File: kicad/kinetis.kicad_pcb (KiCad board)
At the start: 2 copper layers, 88.9 x 88.9 mm, 75 parts, among them J1 USB_Micro_B, J2 JLink_SWD_20pin, J3 CONN_01X16, J4 CONN_01X16, J5 FTDI_Connector, J6 CONN_01X16, J7 CONN_01X16, M1 #4-40 Mounting Hole, M2 #4-40 Mounting Hole, M3 #4-40 Mounting Hole, M4 #4-40 Mounting Hole, SW1 DPDT, SW2 SPST, SW3 SPST, SW4 SPST, SW5 SPST, SW6 SPST, U1 LM1117-ADJ, U2 MKL16Z64VLH4, Y1 12.000 MHz

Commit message: More routing tweaks
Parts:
- moved R28 0.70 mm to (179.5, 134.6)
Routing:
- net GND: track 105.0 -> 137.3 mm, vias 33 -> 42
- net /HEADER_B[12]: track 68.4 -> 69.0 mm

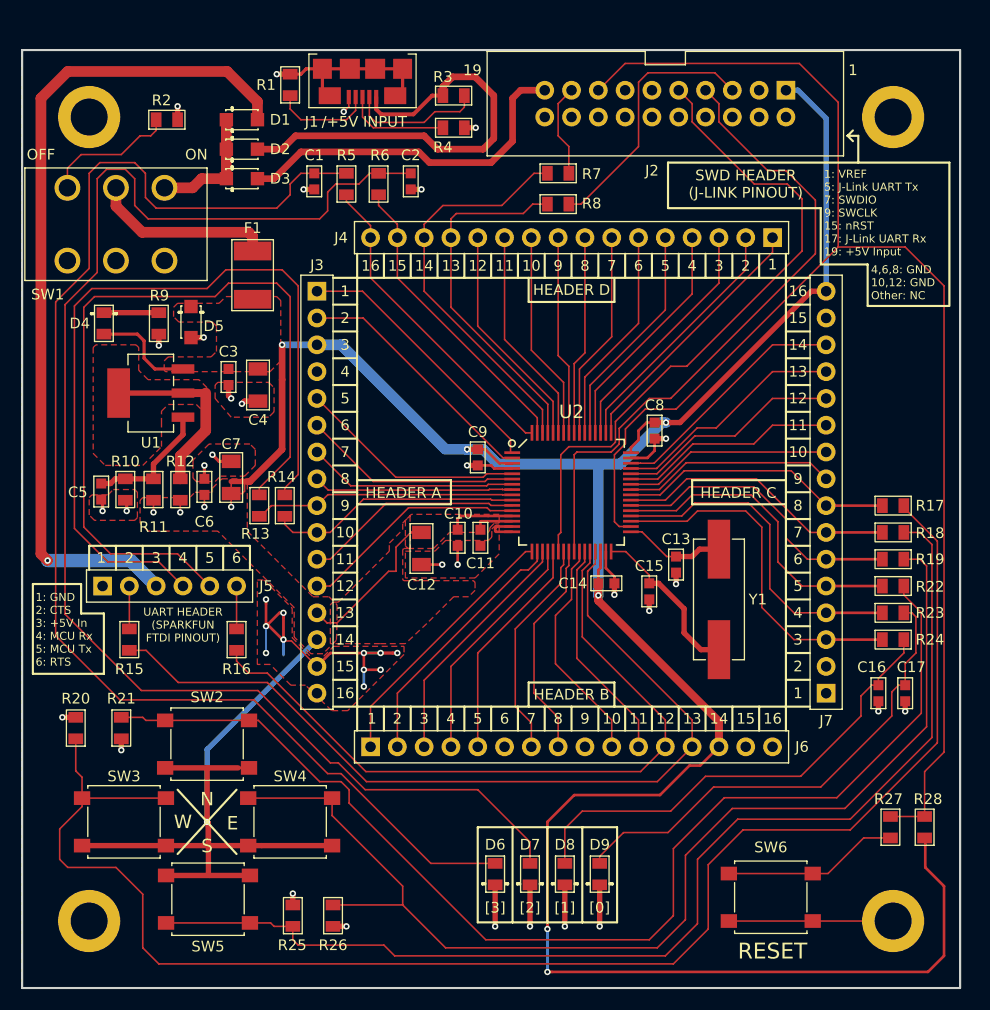
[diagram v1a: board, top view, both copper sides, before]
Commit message: Improved the +3.3V analog section
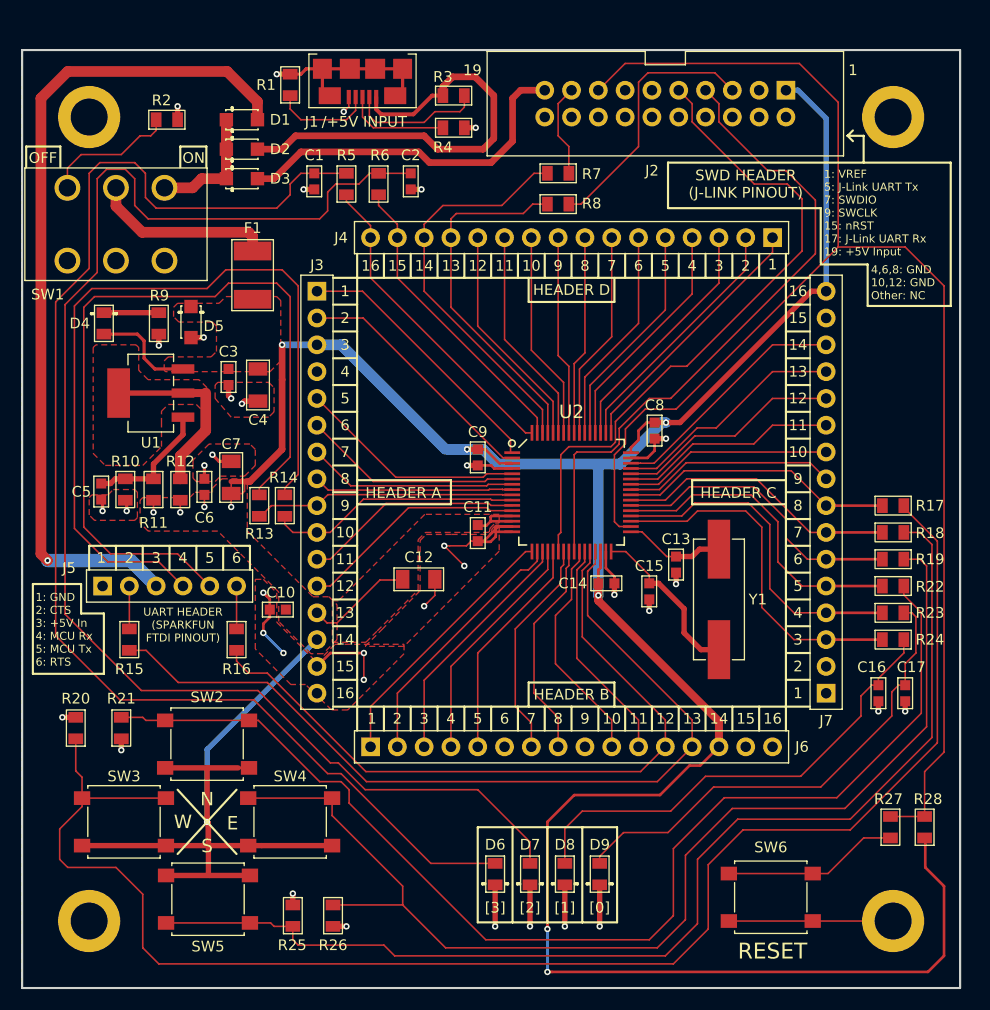
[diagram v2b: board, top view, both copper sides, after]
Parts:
- moved C10 18.4 mm to (118.2, 114.0), turned to 180 degrees
- moved C12 2.93 mm to (131.6, 111.1), turned to 0 degrees
- moved C11 0.51 mm to (137.2, 106.7)
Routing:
- net GND: track 137.3 -> 124.7 mm, vias 42 -> 37
- net +3.3V: track 337.9 -> 329.2 mm
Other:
- net class Default: clearance 0.2032 -> 0.1778
- rule trace_clearance: 0.2032 -> 0.1778

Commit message: Yet more tweaks
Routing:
- net GND: track 124.7 -> 132.4 mm, vias 37 -> 41
- net +3.3V: track 329.2 -> 324.0 mm, vias 11 -> 7

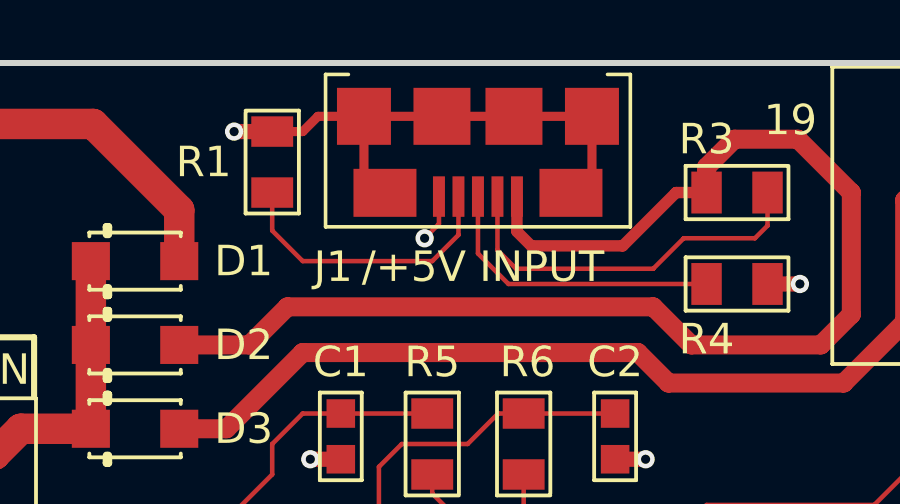
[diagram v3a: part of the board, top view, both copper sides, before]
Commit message: Updated USB 3-D model
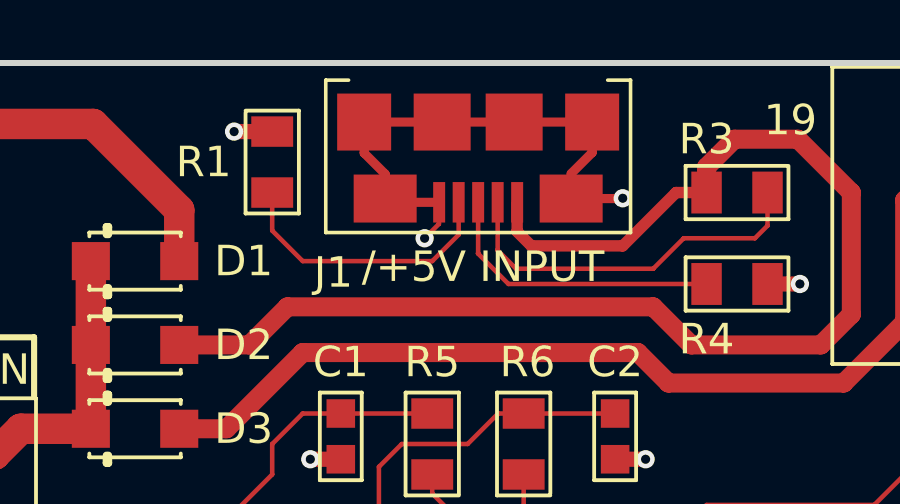
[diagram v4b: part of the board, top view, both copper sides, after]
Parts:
- moved J1 0.19 mm to (126.2, 62.9)
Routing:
- net GND: track 132.4 -> 132.8 mm, vias 41 -> 42

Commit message: Re-applied annotation
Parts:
- renumbered C5 to C1, C9 to C10, C14 to C12, C8 to C13, C15 to C14, C13 to C15, C6 to C2, C7 to C4, C4 to C5, C1 to C6, C10 to C7, C2 to C8, C12 to C9, D4 to D1, D5 to D2, D1 to D3, D2 to D4, D3 to D5, J5 to J1, J3 to J2, J1 to J3, J6 to J4, J2 to J5, J4 to J6, M3 to M2, M2 to M3, R20 to R1, R16 to R10, R13 to R11, R14 to R12, R5 to R13, R6 to R14, R25 to R15, R26 to R16, R3 to R17, R4 to R18, R7 to R19, R8 to R20, R17 to R21, R18 to R22, R19 to R23, R22 to R24, R23 to R25, R24 to R26, R10 to R3, R9 to R4, R11 to R5, R15 to R6, R21 to R7, R12 to R8, R1 to R9, SW3 to SW2, SW2 to SW3, SW5 to SW4, SW4 to SW5

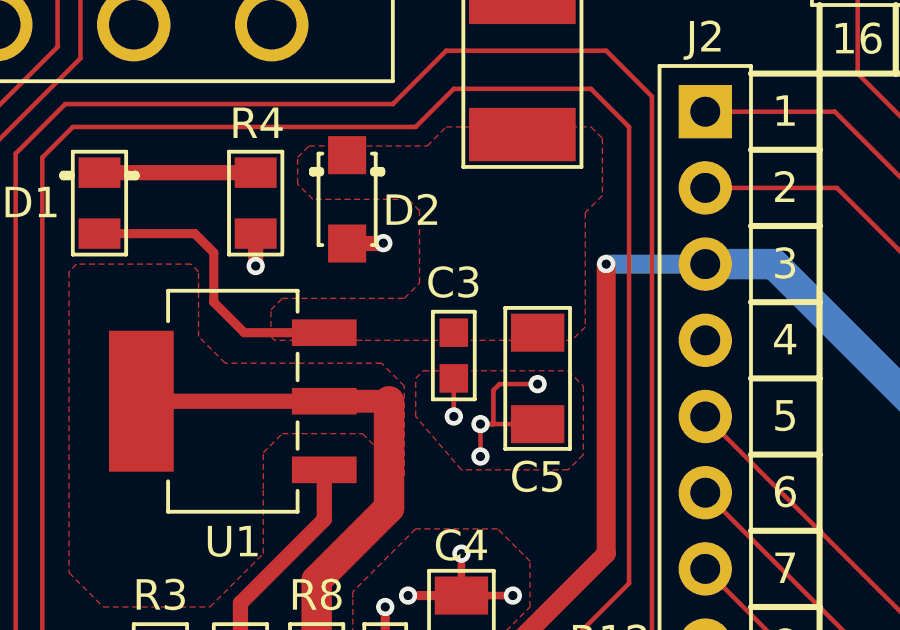
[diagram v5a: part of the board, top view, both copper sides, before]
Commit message: Updated SOD-123 footprint. Cleaned up fab drawing.
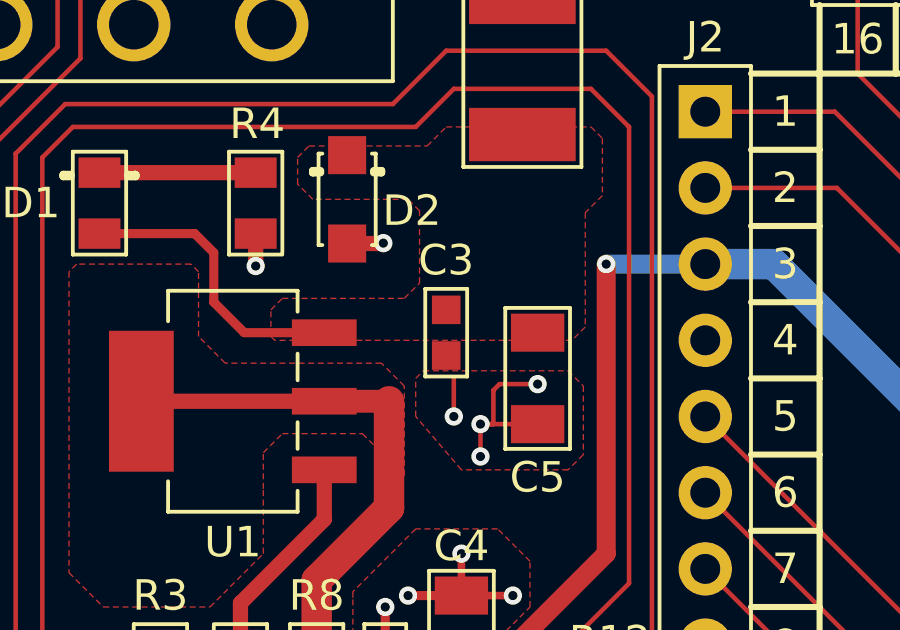
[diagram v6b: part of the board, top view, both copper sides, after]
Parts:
- moved C3 0.80 mm to (113.3, 91.2)

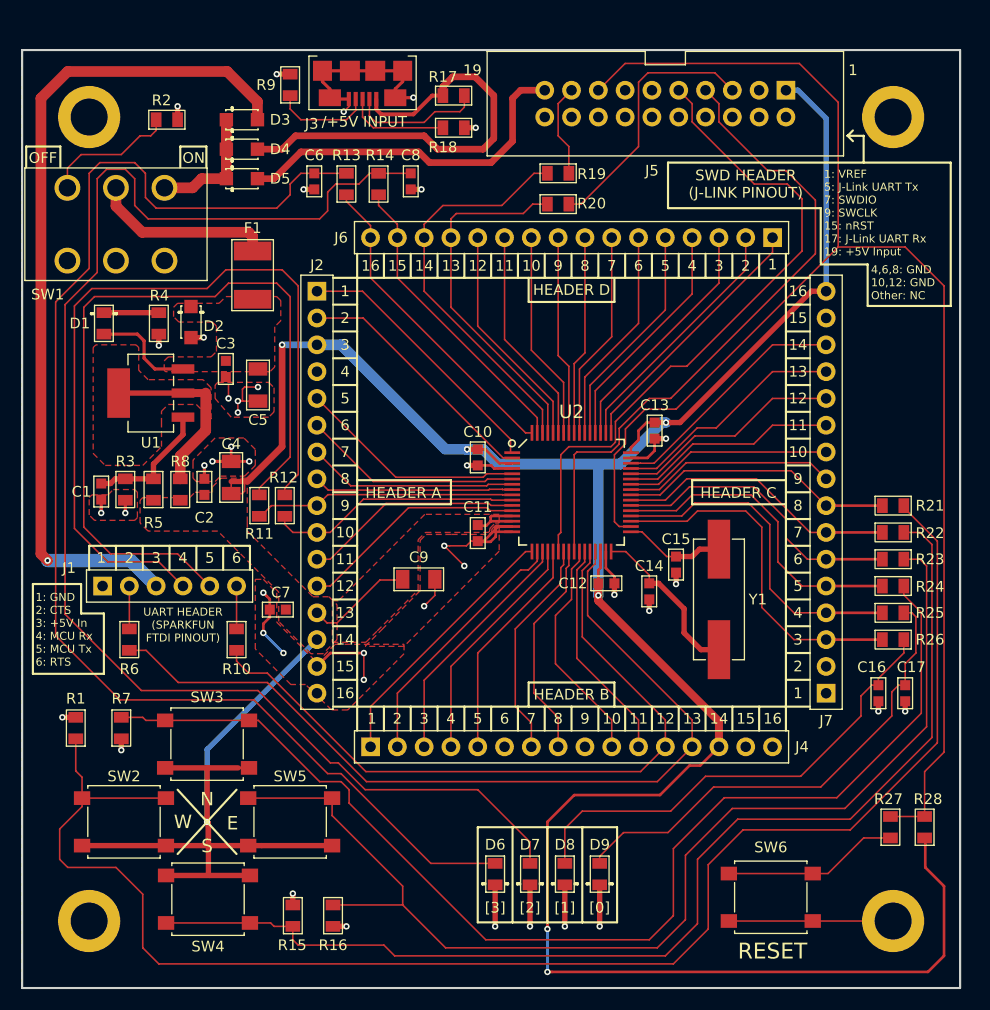
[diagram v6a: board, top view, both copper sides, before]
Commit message: Changed USB connector. Fixed soldermask clearance settings.
This commit changes the USB connector from an SMT-only connector
to one with some through-hole mounting tabs. This should help to
provide mechanical ruggedness for the board.

This commit also fixed the soldermask clearance settings so that the
USB connector and Kinets both have soldermask in-between the pins.
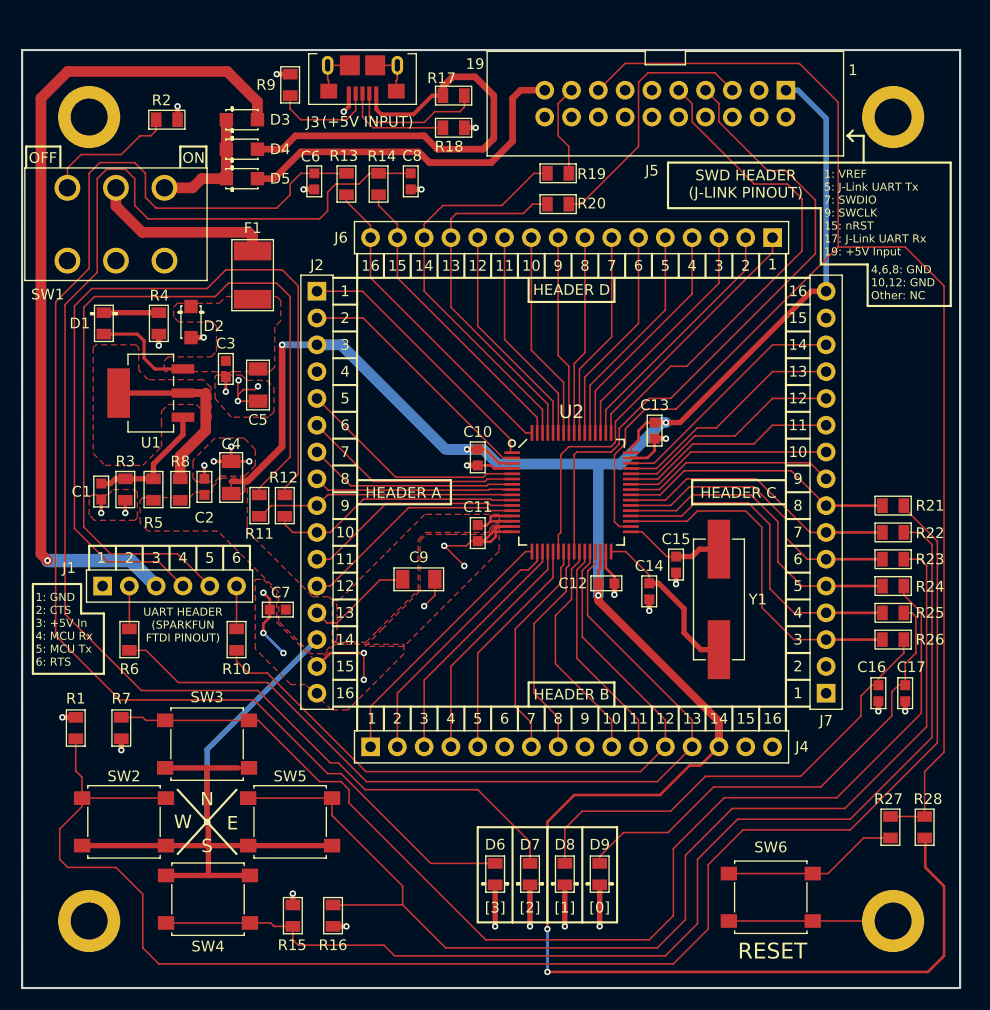
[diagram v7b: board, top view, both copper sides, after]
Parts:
- J3: footprint custom_footprints:10118192-0001LF -> custom_footprints:10118193-0001LF
- moved J3 0.52 mm to (126.2, 62.4)
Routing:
- net GND: track 132.8 -> 125.5 mm, vias 42 -> 41
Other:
- rule pad_to_mask_clearance: 0.2 -> 0.1016
- board text added: "(+5V INPUT)"
- board text removed: "/+5V INPUT"

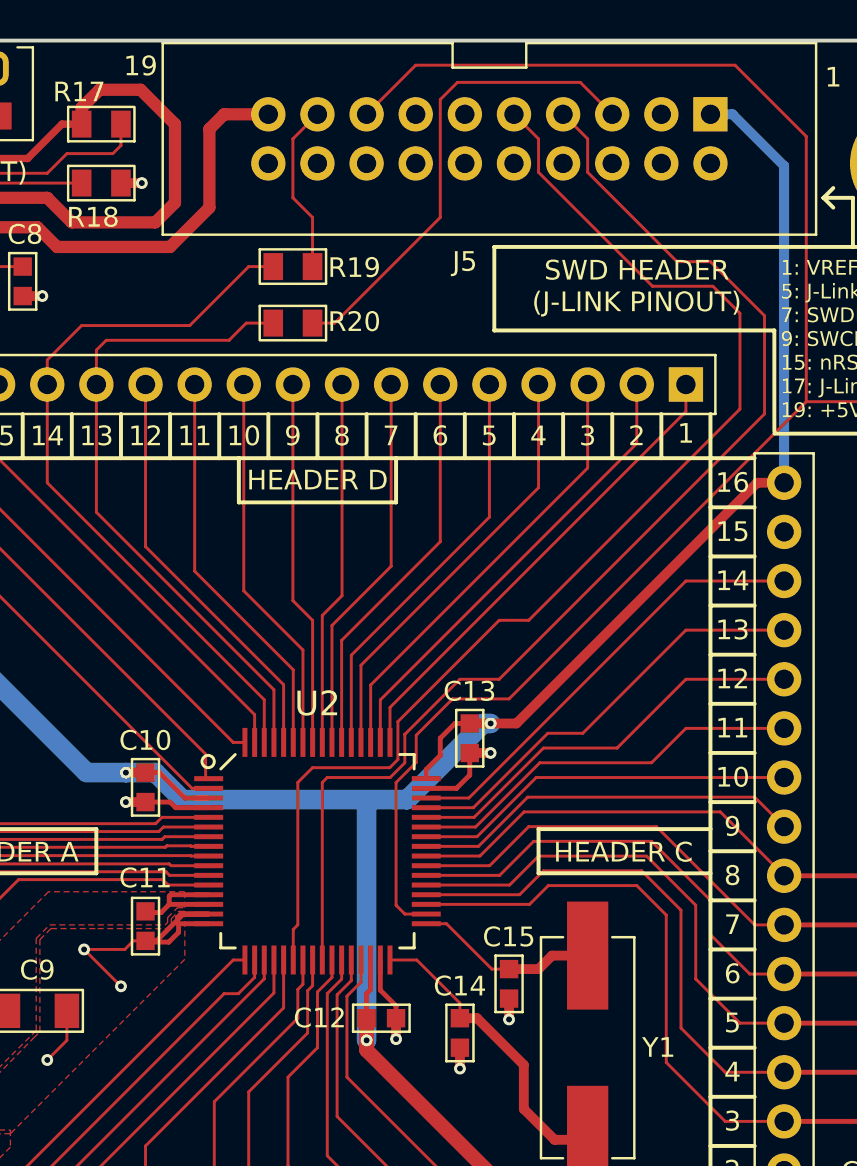
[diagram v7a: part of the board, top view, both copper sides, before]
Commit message: Bugfix to USB 3D model. Added ground stitches.
This commit fixes the selection of the USB connector's 3D model.
It also adds some small ground patches over the 3.3V disruptions
under the Kinetis.
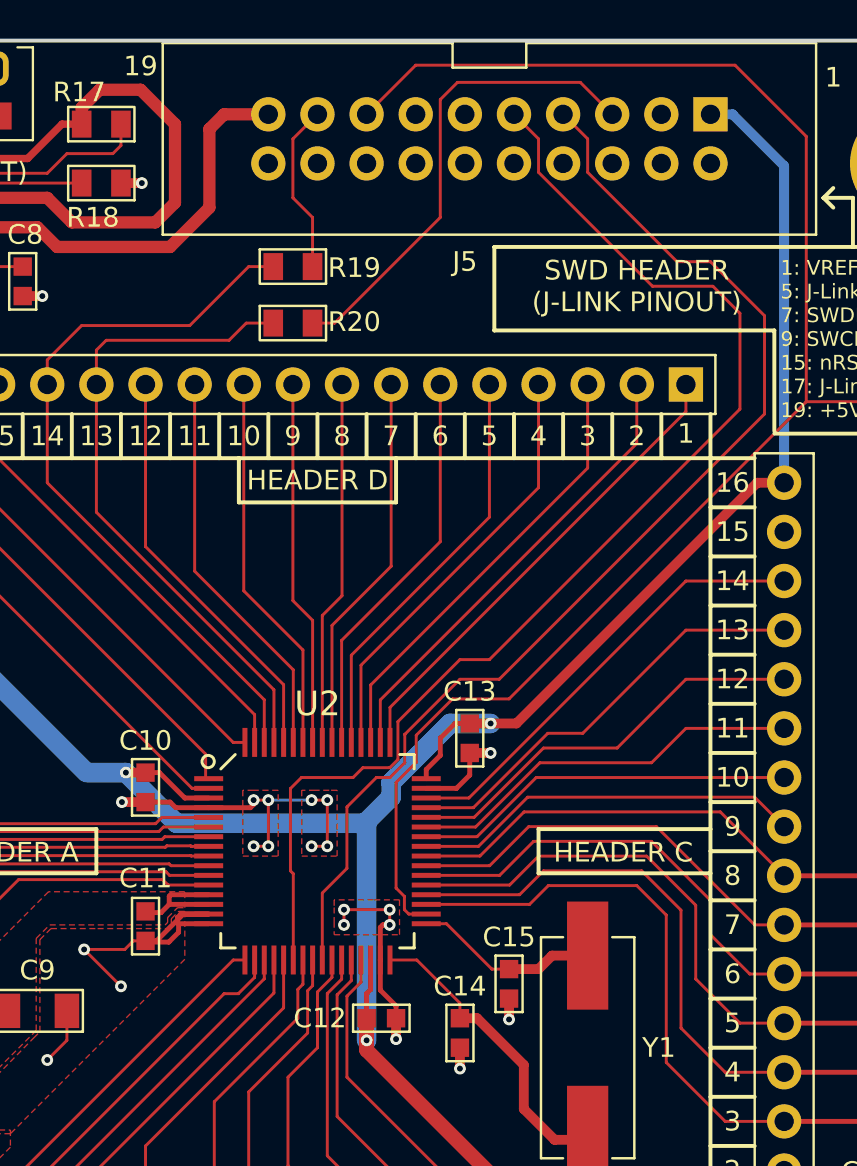
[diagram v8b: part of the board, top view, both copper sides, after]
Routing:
- net GND: track 125.5 -> 144.6 mm, vias 41 -> 53
- net JLink_SWDIO: track 61.6 -> 60.1 mm
- net +3.3V: track 324.0 -> 323.1 mm
